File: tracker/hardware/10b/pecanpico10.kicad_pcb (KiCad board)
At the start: 2 copper layers, 23 x 50 mm, 119 parts, among them IC1 SPV1040T, IC10 AS213-92LF, IC2 TPS62260DRVR, IC3 ADP322ACPZ-115-R7, IC4 Si4464-B1B-FM, IC5 STM32F413RHT6, IC6 EVA-7M or EVA-M8, IC7 PAC1720-1-AIA-TR, IC8 TPS62260DRVR, IC9 BME280, J1 DM3AT-SF-PEJM5, J2 CONN_01X15, P1 CONN_01X25, P3 ZX62-B-5PA(33), P4 SMA, Q1 FDN306P, X1 KT2016K26000BCW18ZAS, X2 SF2316H

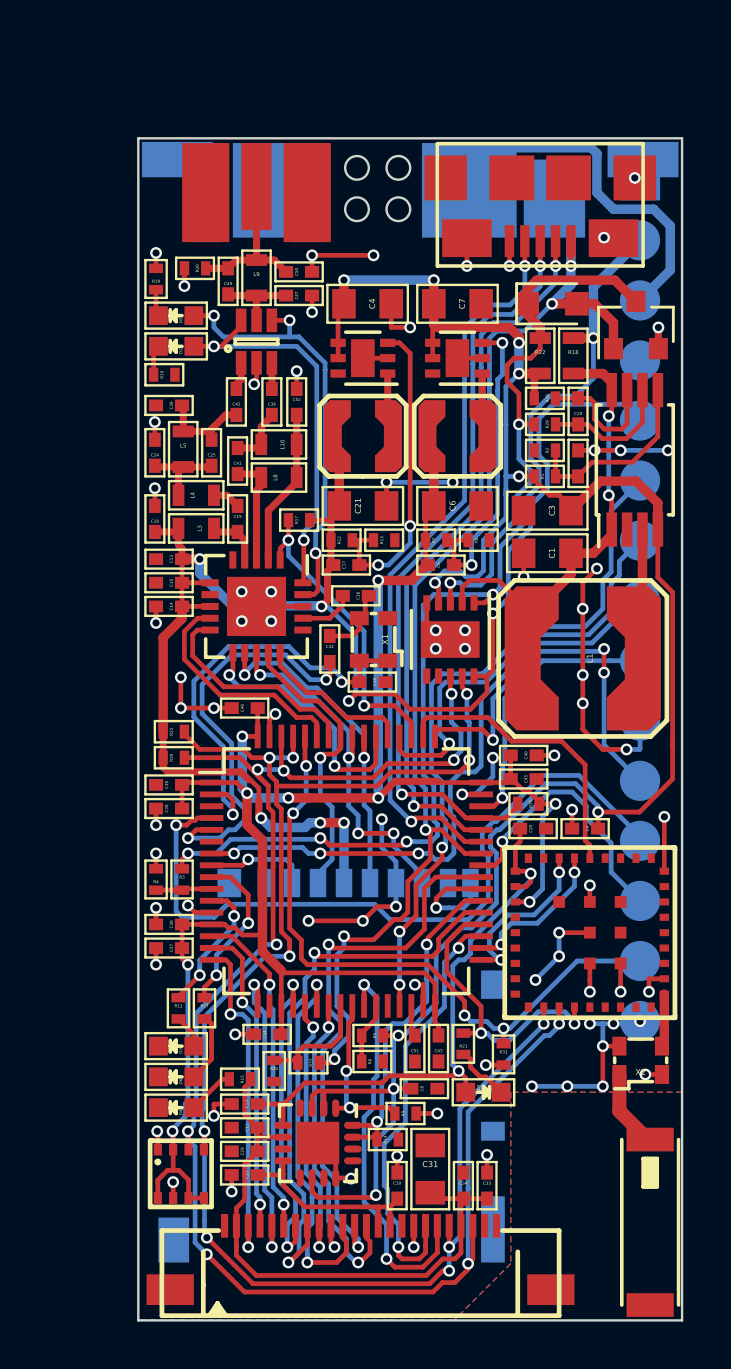
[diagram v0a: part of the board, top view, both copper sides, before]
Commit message: Moved wires around, added vias, created GERBERs for 10b
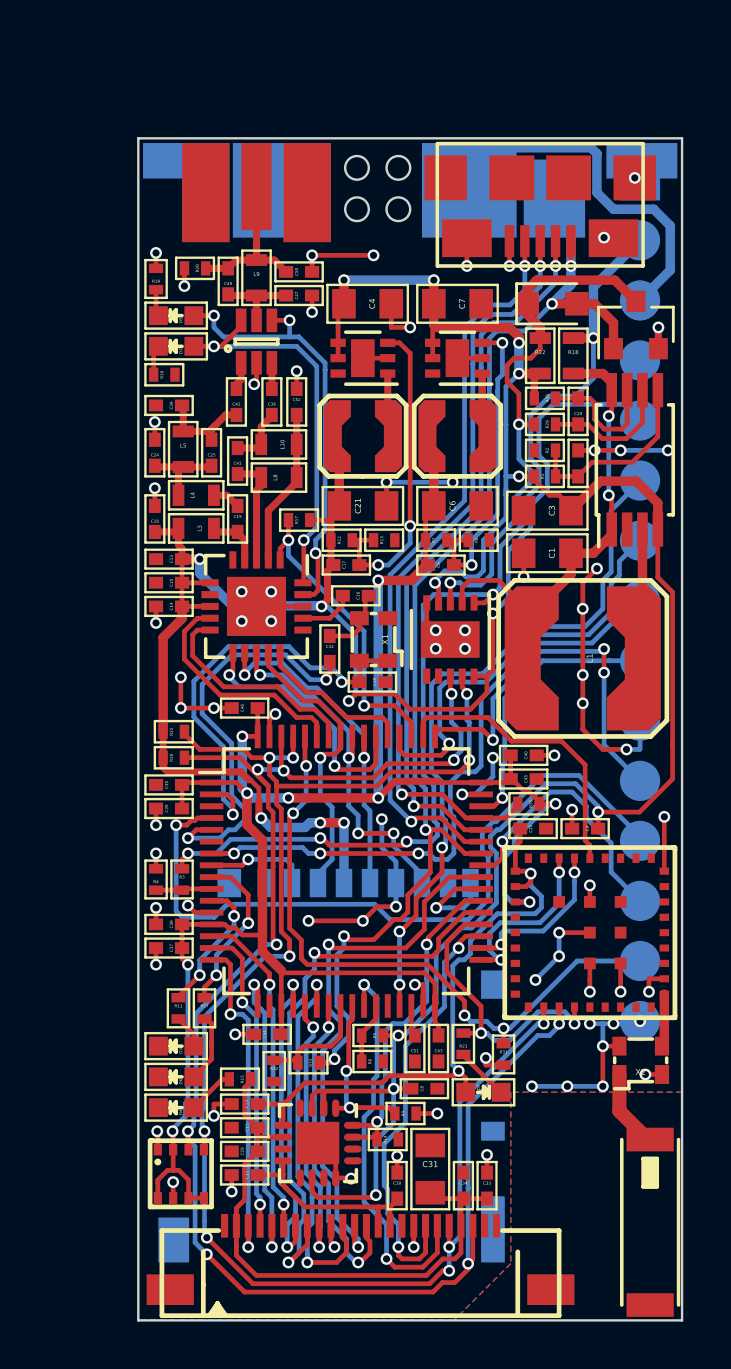
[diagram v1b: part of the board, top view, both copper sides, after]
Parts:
- moved W2 0.07 mm to (48.8, 75.5)
- moved W3 0.07 mm to (68.4, 75.5)
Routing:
- net VCC: track 82.9 -> 84.4 mm
- net /VCC_GPS: track 25.0 -> 26.4 mm

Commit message: Renamed power nets, added comments to schematic, exported schematic and 3D pictures to PDF
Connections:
- net /TCXO_EN renamed +TCXO
- net /VCC_GPS renamed +GPS
- net VCC renamed +3V0
